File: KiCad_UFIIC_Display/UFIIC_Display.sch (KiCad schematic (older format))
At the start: 36 parts, among them J1 I2C, J2 SWD, Q1 BC639, Q2 BSS138, Q3 BSS138, Q4 BC547, SW1 SW_Push, U1 AMS1117-3.3, U2 STM32F030F4P6, U3 HD44780

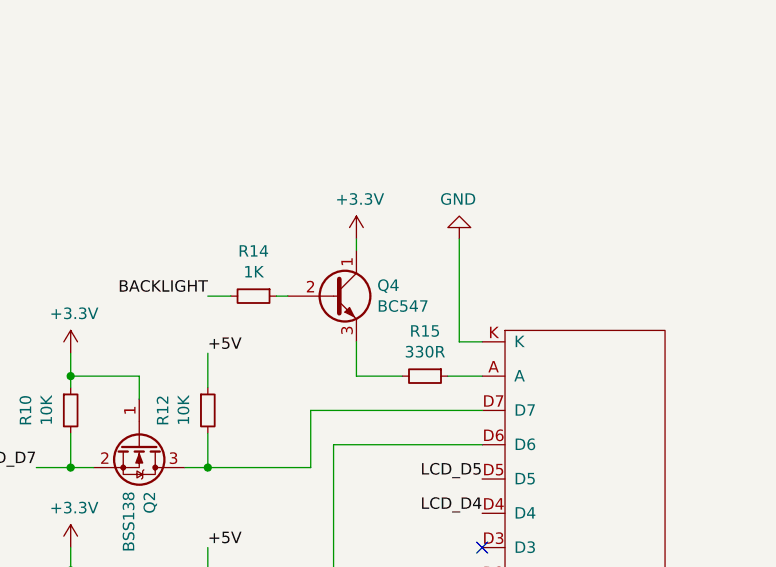
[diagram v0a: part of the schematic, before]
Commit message: Backlight powered by 5V step up
+ backlight is powered by 5V step-up
+ removed unnecessary KiCad files
+ updated .gitignore
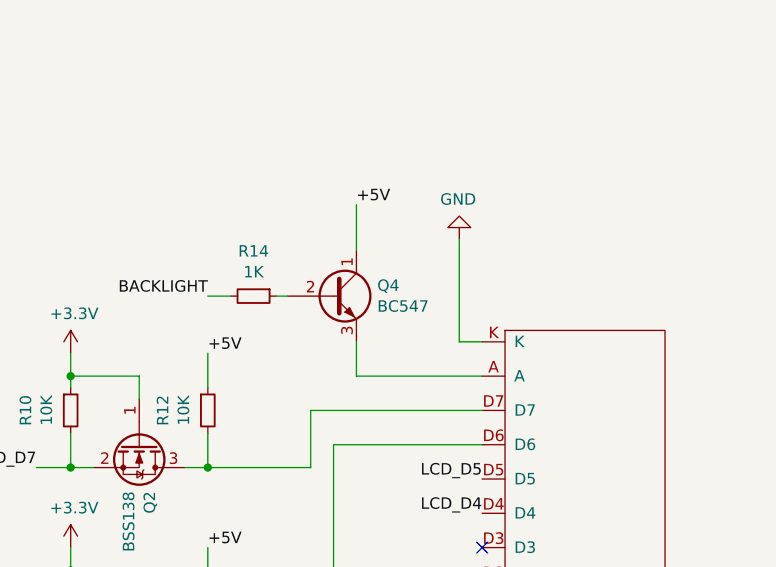
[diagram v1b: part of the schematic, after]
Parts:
- removed R15: 330R, Resistor_SMD:R_1206_3216Metric, symbol Device:R_Small
- removed U3: HD44780, WK_lib:HD44780, symbol UFIIC_Display-rescue:HD44780-WK_lib
- added U3: HD44780, WK_lib:HD44780, symbol WK_lib:HD44780
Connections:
- net +3V3: no longer Q4.1 (C)
- net +5V: now also Q4.1 (C)
- net GND: now also U3.GND, U3.K
- net LCD_D4: now also U3.D4
- net LCD_D5: now also U3.D5
- net LCD_E: now also U3.E
- net LCD_RS: now also U3.RS
- net LCD_RW: now also U3.RW
- net at Q4.3 (E): now also U3.A
- net at Q3.3 (D), R13.2: now also U3.D6
- net at Q2.3 (D), R12.2: now also U3.D7
- net at RV1.2: now also U3.V0
- net at RV1.3: now also U3.VCC
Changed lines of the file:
@@
 Wire Wire Line
 	8800 2650 8850 2650
-$Comp
-L Device:R_Small R15
-U 1 1 5EEA1330
-P 9450 3000
-F 0 "R15" V 9254 3000 50  0000 C CNN
-F 1 "330R" V 9345 3000 50  0000 C CNN
-F 2 "Resistor_SMD:R_1206_3216Metric" H 9450 3000 50  0001 C CNN
-F 3 "~" H 9450 3000 50  0001 C CNN
-	1    9450 3000
-	0    1    1    0
-$EndComp
-Wire Wire Line
-	9700 3000 9550 3000
-$Comp
-L power:+3.3V #PWR016
-U 1 1 5EEA34D9
-P 9150 2400
-F 0 "#PWR016" H 9150 2250 50  0001 C CNN
-F 1 "+3.3V" H 9165 2573 50  0000 C CNN
-F 2 "" H 9150 2400 50  0001 C CNN
-F 3 "" H 9150 2400 50  0001 C CNN
-	1    9150 2400
-	1    0    0    -1
-$EndComp
-Wire Wire Line
-	9150 2450 9150 2400
 Wire Wire Line
 	9600 2400 9600 2850
 Wire Wire Line
 	9150 2850 9150 3000
-Wire Wire Line
-	9150 3000 9350 3000
 $Comp
 L power:GND #PWR017
@@
 $EndComp
 $Comp
-L UFIIC_Display-rescue:HD44780-WK_lib U3
-U 1 1 5EE8760B
-P 10200 3900
-F 0 "U3" H 10528 3876 50  0000 L CNN
-F 1 "HD44780" H 10528 3785 50  0000 L CNN
-F 2 "WK_lib:HD44780" H 10200 3800 50  0001 C CNN
-F 3 "" H 10200 3900 50  0001 C CNN
-	1    10200 3900
-	1    0    0    -1
-$EndComp
-$Comp
 L Device:Q_NPN_BCE Q1
 U 1 1 5EEC50BD
@@
 Wire Wire Line
 	8500 4250 9050 4250
+Text Label 9150 2250 0    50   ~ 0
++5V
+Wire Wire Line
+	9150 2250 9150 2450
+Wire Wire Line
+	9150 3000 9700 3000
+$Comp
+L WK_lib:HD44780 U3
+U 1 1 5F0B845F
+P 10200 3900
+F 0 "U3" H 10528 3876 50  0000 L CNN
+F 1 "HD44780" H 10528 3785 50  0000 L CNN
+F 2 "WK_lib:HD44780" H 10200 3800 50  0001 C CNN
+F 3 "" H 10200 3900 50  0001 C CNN
+	1    10200 3900
+	1    0    0    -1
+$EndComp
 $EndSCHEMATC
